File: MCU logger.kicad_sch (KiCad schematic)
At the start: 0 parts

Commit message: added a resistor
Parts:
- added R1: R, symbol Device:R
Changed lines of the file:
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@@
 	(generator_version "10.99")
 	(paper "A4")
+	(symbol
+		(lib_id "Device:R")
+		(at 106.68 85.09 0)
+		(unit 1)
+		(body_style 1)
+		(exclude_from_sim no)
+		(in_bom yes)
+		(on_board yes)
+		(in_pos_files yes)
+		(dnp no)
+		(fields_autoplaced yes)
+		(property "Reference" "R1"
+			(at 109.22 83.8199 0)
+			(show_name no)
+			(do_not_autoplace no)
+			(effects
+				(font
+					(size 1.27 1.27)
+				)
+				(justify left)
+			)
+		)
+		(property "Value" "R"
+			(at 109.22 86.3599 0)
+			(show_name no)
+			(do_not_autoplace no)
+			(effects
+				(font
+					(size 1.27 1.27)
+				)
+				(justify left)
+			)
+		)
+		(property "Footprint" ""
+			(at 104.902 85.09 90)
+			(hide yes)
+			(show_name no)
+			(do_not_autoplace no)
+			(effects
+				(font
+					(size 1.27 1.27)
+				)
+			)
+		)
+		(property "Datasheet" ""
+			(at 106.68 85.09 0)
+			(hide yes)
+			(show_name no)
+			(do_not_autoplace no)
+			(effects
+				(font
+					(size 1.27 1.27)
+				)
+			)
+		)
+		(property "Description" "Resistor"
+			(at 106.68 85.09 0)
+			(hide yes)
+			(show_name no)
+			(do_not_autoplace no)
+			(effects
+				(font
+					(size 1.27 1.27)
+				)
+			)
+		)
+		(pin "1"
+		)
+		(pin "2"
+		)
+		(instances
+			(project "MCU logger"
+				(path "/f2d4402a-bfbf-4d69-9a4a-bfc17a890c47"
+					(reference "R1")
+					(unit 1)
+				)
+			)
+		)
+	)
 	(sheet_instances
 		(path "/"

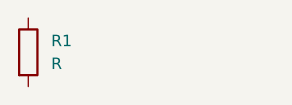
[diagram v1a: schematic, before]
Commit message: added the capacitor
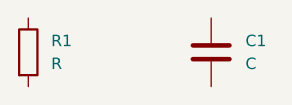
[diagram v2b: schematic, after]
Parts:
- added C1: C, symbol Device:C
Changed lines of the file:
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@@
+		)
+	)
+	(symbol
+		(lib_id "Device:C")
+		(at 127 85.09 0)
+		(unit 1)
+		(body_style 1)
+		(exclude_from_sim no)
+		(in_bom yes)
+		(on_board yes)
+		(in_pos_files yes)
+		(dnp no)
+		(fields_autoplaced yes)
+		(property "Reference" "C1"
+			(at 130.81 83.8199 0)
+			(show_name no)
+			(do_not_autoplace no)
+			(effects
+				(font
+					(size 1.27 1.27)
+				)
+				(justify left)
+			)
+		)
+		(property "Value" "C"
+			(at 130.81 86.3599 0)
+			(show_name no)
+			(do_not_autoplace no)
+			(effects
+				(font
+					(size 1.27 1.27)
+				)
+				(justify left)
+			)
+		)
+		(property "Footprint" ""
+			(at 127.9652 88.9 0)
+			(hide yes)
+			(show_name no)
+			(do_not_autoplace no)
+			(effects
+				(font
+					(size 1.27 1.27)
+				)
+			)
+		)
+		(property "Datasheet" ""
+			(at 127 85.09 0)
+			(hide yes)
+			(show_name no)
+			(do_not_autoplace no)
+			(effects
+				(font
+					(size 1.27 1.27)
+				)
+			)
+		)
+		(property "Description" "Unpolarized capacitor"
+			(at 127 85.09 0)
+			(hide yes)
+			(show_name no)
+			(do_not_autoplace no)
+			(effects
+				(font
+					(size 1.27 1.27)
+				)
+			)
+		)
+		(pin "1"
+		)
+		(pin "2"
+		)
+		(instances
+			(project "MCU logger"
+				(path "/f2d4402a-bfbf-4d69-9a4a-bfc17a890c47"
+					(reference "C1")
+					(unit 1)
+				)
+			)
 		)
 	)

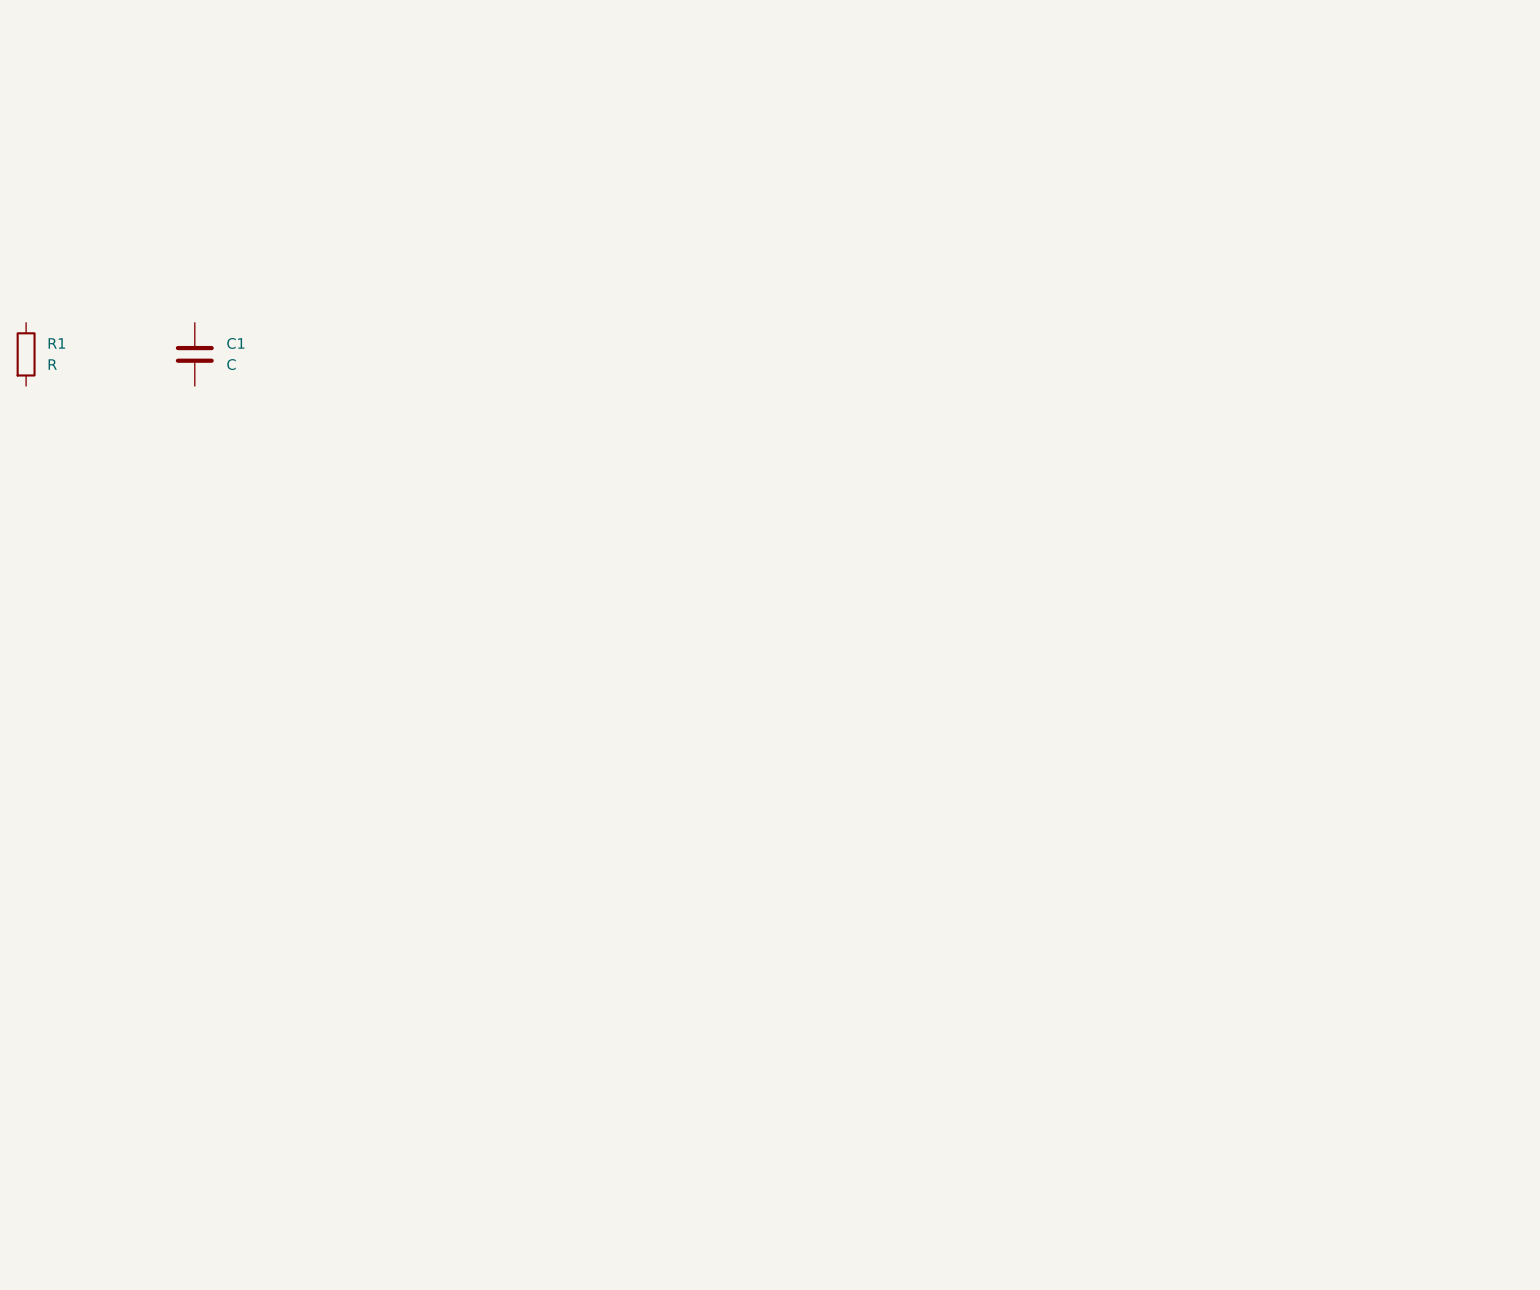
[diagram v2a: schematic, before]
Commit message: added required symbols
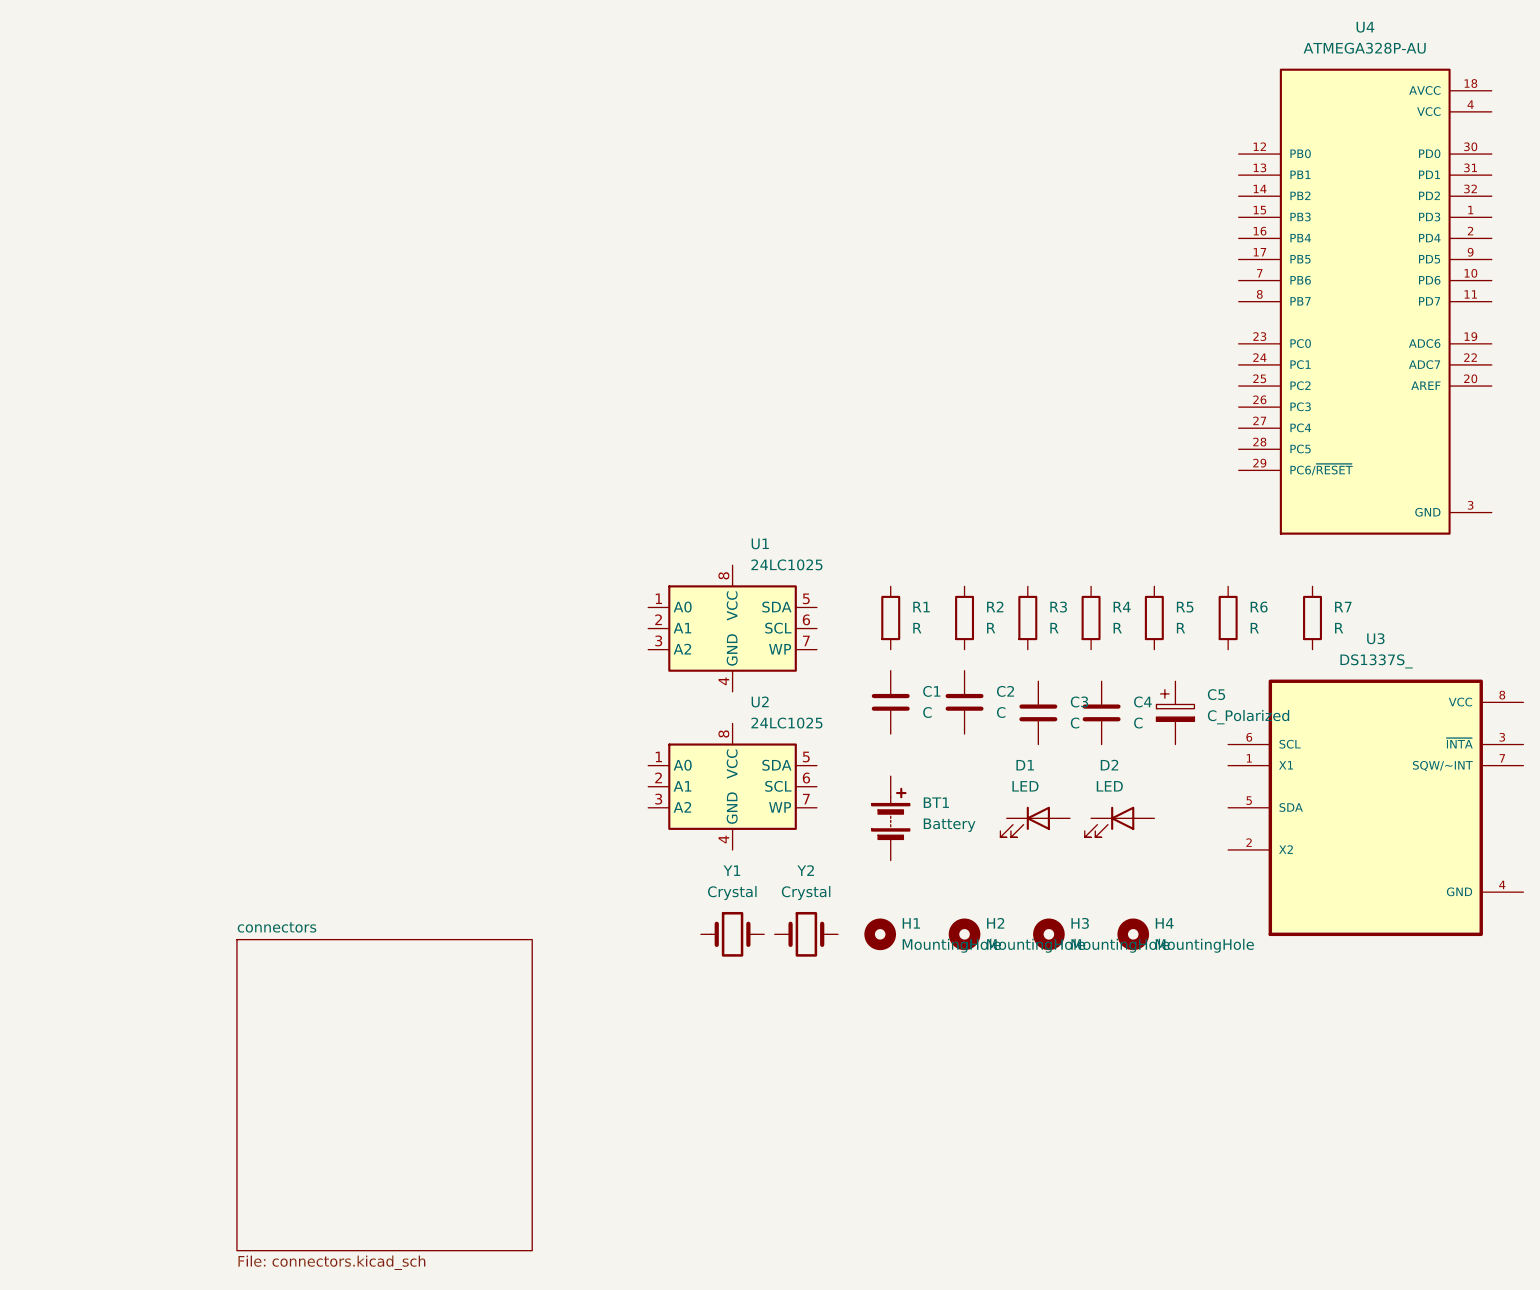
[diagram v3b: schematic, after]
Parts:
- added BT1: Battery, symbol Device:Battery
- added C2, C3, C4: C, symbol Device:C
- added C5: C_Polarized, symbol Device:C_Polarized
- added D1, D2: LED, symbol Device:LED
- added H1, H2, H3, H4: MountingHole, symbol Mechanical:MountingHole
- added R2, R3, R4, R5, R6, R7: R, symbol Device:R
- added U1, U2: 24LC1025, symbol Memory_EEPROM:24LC1025
- added U3: DS1337S_, DS1337S_:SOIC127P600X175-8N, symbol DS1337S_:DS1337S_
- added U4: ATMEGA328P-AU, ATMEGA328P-AU:QFP80P900X900X120-32N, symbol ATMEGA328P-AU:ATMEGA328P-AU
- added Y1, Y2: Crystal, symbol Device:Crystal
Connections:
- new net GND: U4.21 (GND), U4.3 (GND), U4.5 (GND)
- new net VCC: U4.4 (VCC), U4.6 (VCC)
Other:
- added sheet connectors (connectors.kicad_sch)
- company: (none) -> Rishikesh Sharma
- title: (none) -> ${prjn}
